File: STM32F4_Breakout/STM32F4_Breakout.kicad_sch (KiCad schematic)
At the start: 28 parts

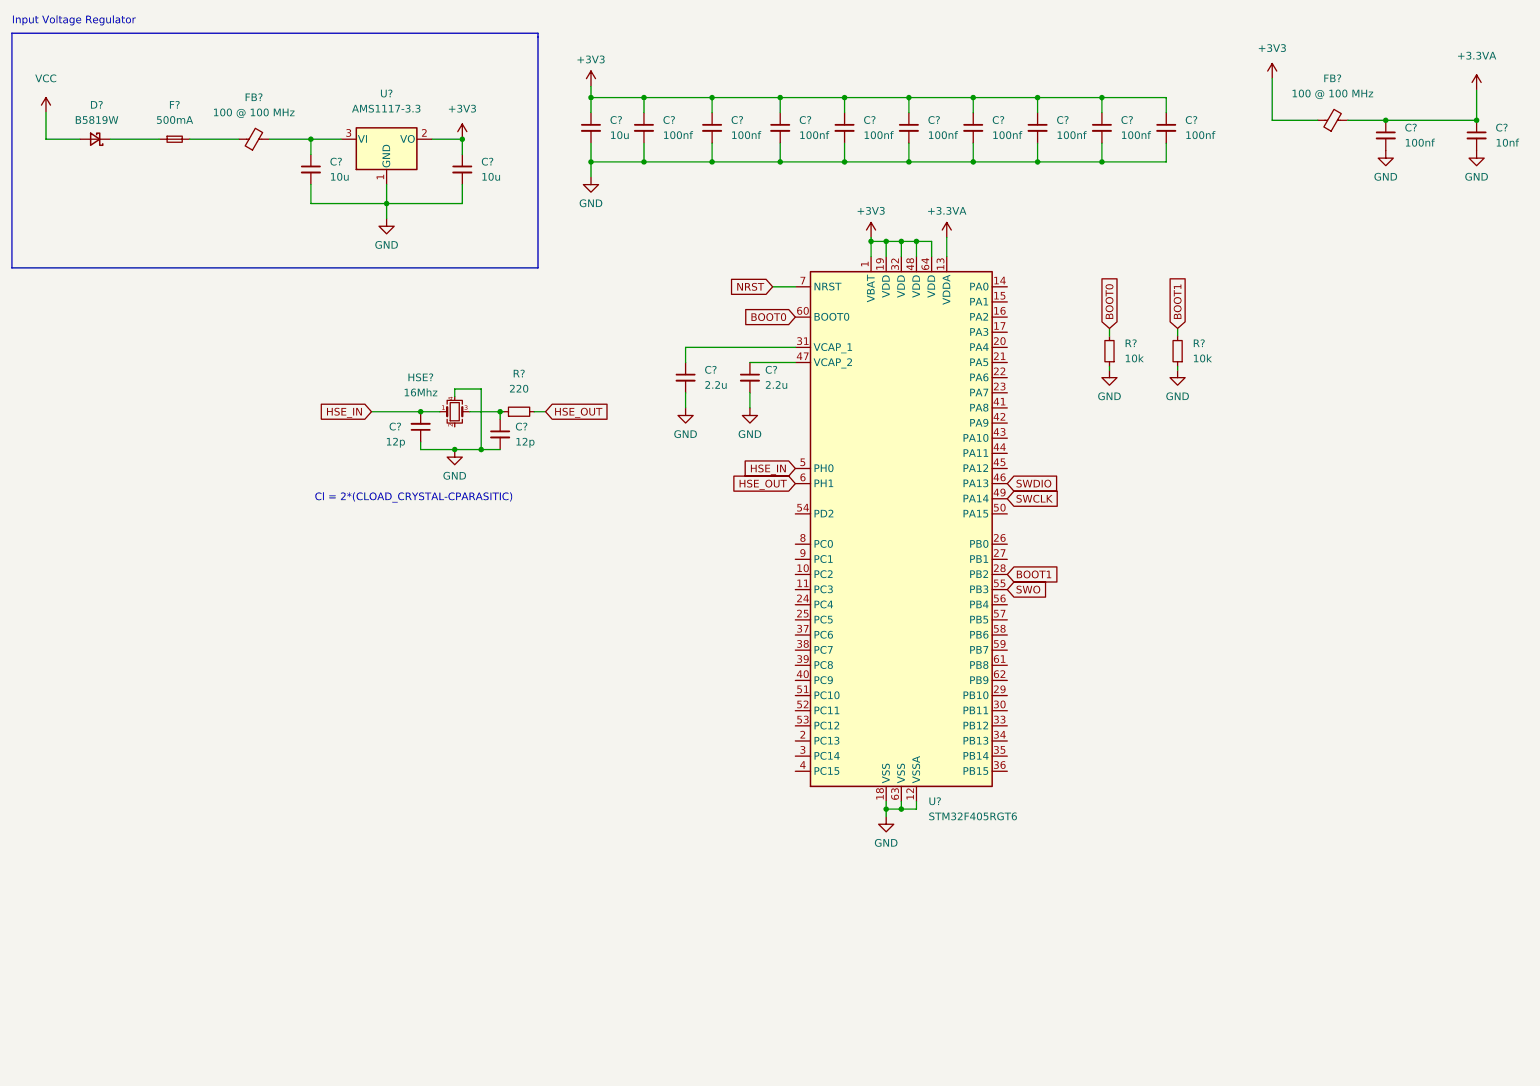
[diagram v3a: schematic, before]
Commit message: serial wire debug; pin assignments and peripheral selection in CubeMX
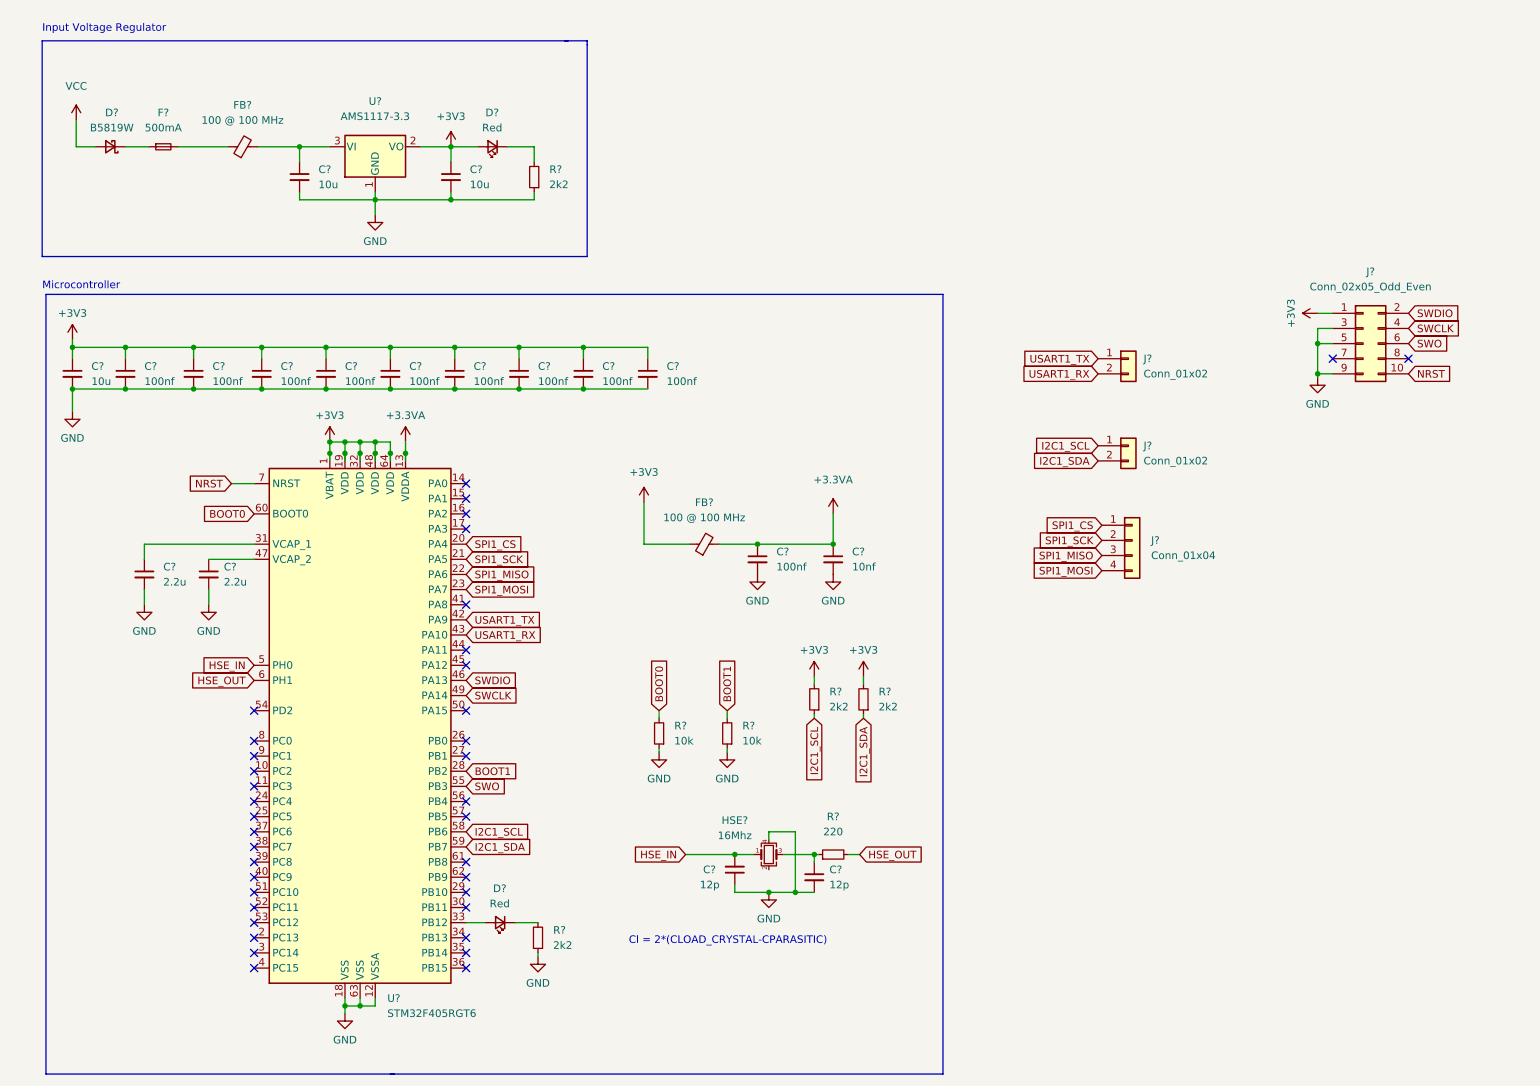
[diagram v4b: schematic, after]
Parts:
- added D? (x2): Red, symbol Device:LED_Small
- added J?: Conn_02x05_Odd_Even, symbol Connector_Generic:Conn_02x05_Odd_Even
- added J? (x2): Conn_01x02, symbol Connector_Generic:Conn_01x02
- added J?: Conn_01x04, symbol Connector_Generic:Conn_01x04
- added R? (x4): 2k2, symbol Device:R_Small
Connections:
- net +3V3: now also D?.2 (A), J?.1 (Pin_1), R?.2, R?.2
- net GND: now also J?.3 (Pin_3), J?.5 (Pin_5), J?.9 (Pin_9), R?.1, R?.1
- net NRST: now also J?.10 (Pin_10)
- net SWCLK: now also J?.4 (Pin_4)
- net SWDIO: now also J?.2 (Pin_2)
- net SWO: now also J?.6 (Pin_6)
- net SPI1_CS: now reaches U?.20 (PA4)
- net SPI1_CS: now also J?.1 (Pin_1)
- net SPI1_SCK: now reaches U?.21 (PA5)
- net SPI1_SCK: now also J?.2 (Pin_2)
- net SPI1_MISO: now reaches U?.22 (PA6)
- net SPI1_MISO: now also J?.3 (Pin_3)
- net SPI1_MOSI: now reaches U?.23 (PA7)
- net SPI1_MOSI: now also J?.4 (Pin_4)
- net at U?.33 (PB12): now also D?.2 (A)
- net USART1_TX: now reaches U?.42 (PA9)
- net USART1_TX: now also J?.1 (Pin_1)
- net USART1_RX: now reaches U?.43 (PA10)
- net USART1_RX: now also J?.2 (Pin_2)
- net I2C1_SCL: now reaches U?.58 (PB6)
- net I2C1_SCL: now also J?.1 (Pin_1), R?.1
- net I2C1_SDA: now reaches U?.59 (PB7)
- net I2C1_SDA: now also J?.2 (Pin_2), R?.1
- new net: D?.1 (K), R?.2 (x2)
- no-connect marks 0 -> 38
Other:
- note added: "Microcontroller"
- moved on the sheet: C?, D?, F?, FB?, HSE?, R?, U?

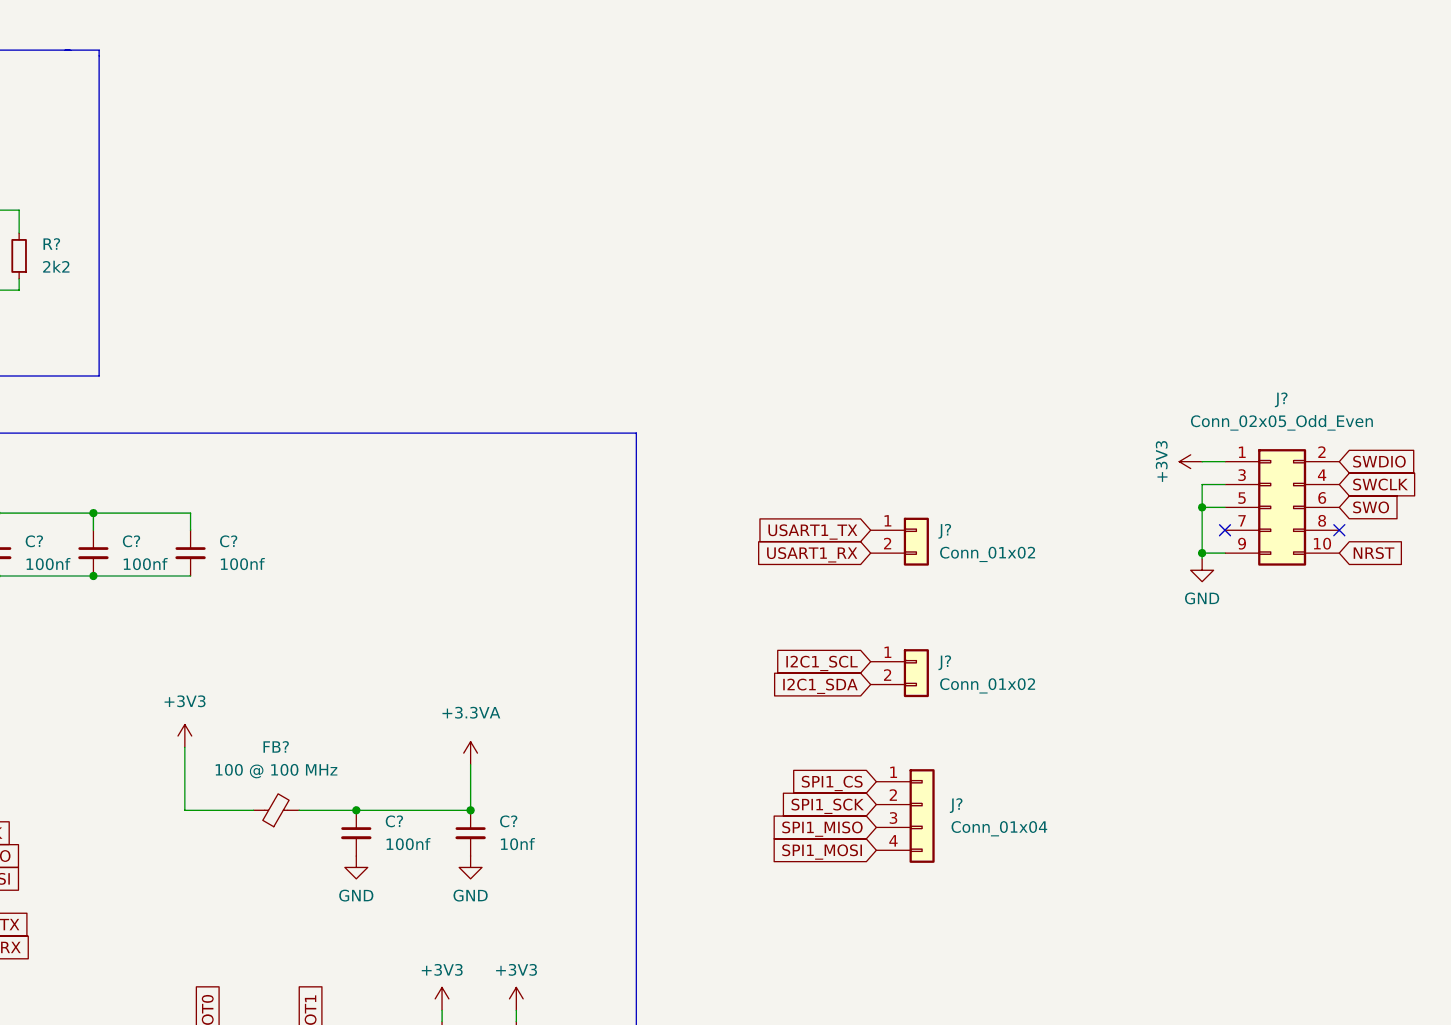
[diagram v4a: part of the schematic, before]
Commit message: adding connectors, test points and mounting holes
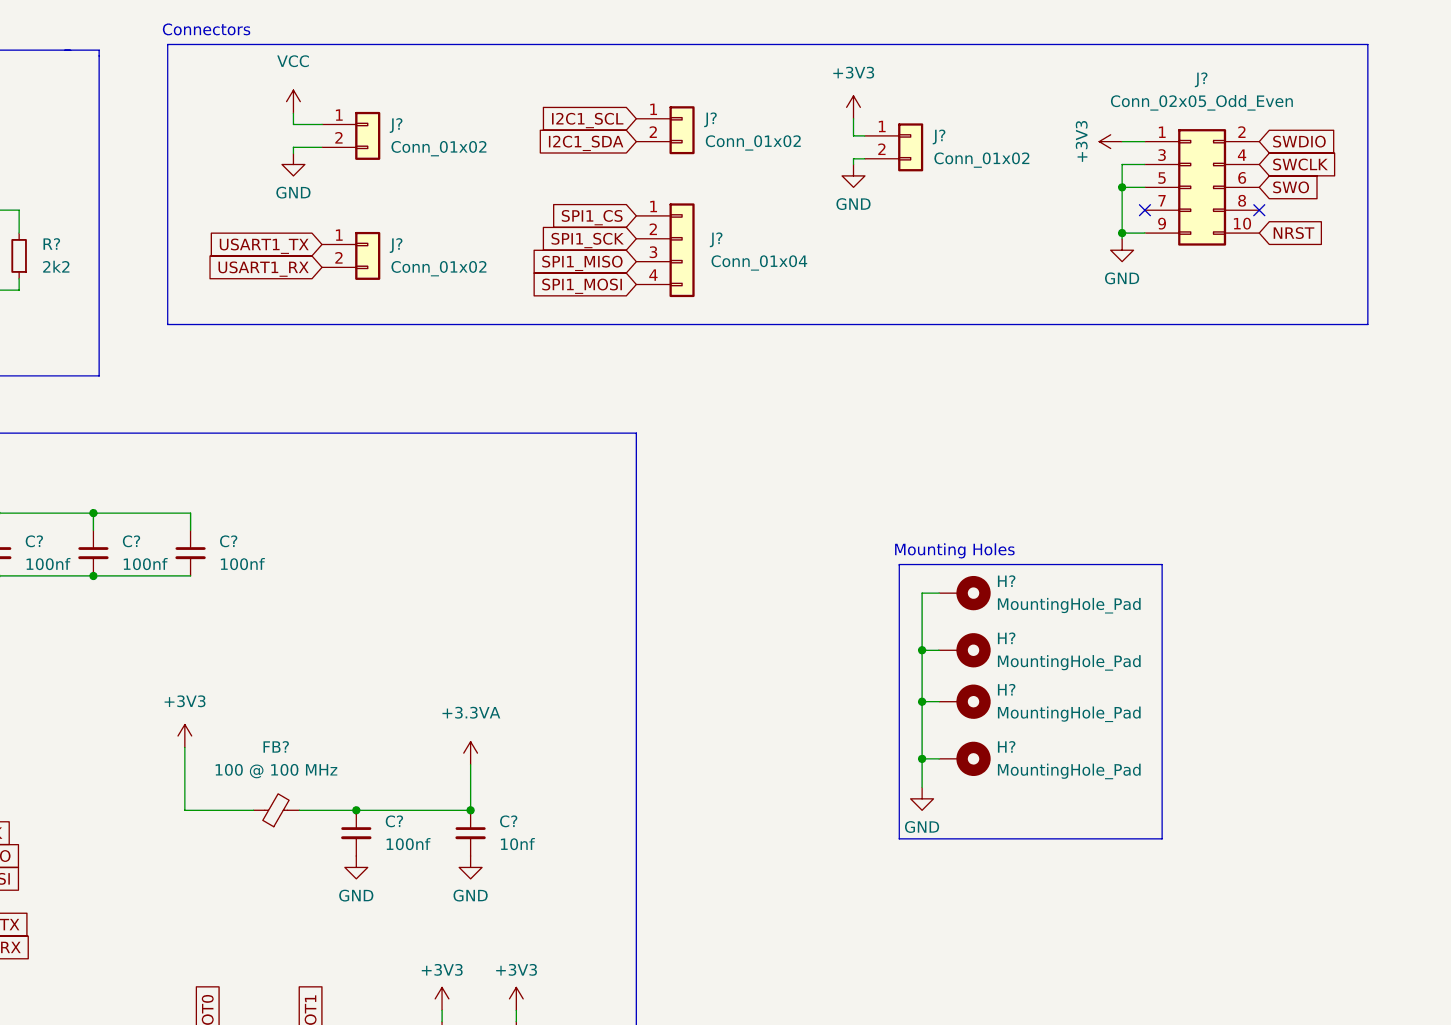
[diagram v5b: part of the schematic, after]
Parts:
- added H? (x4): MountingHole_Pad, symbol Mechanical:MountingHole_Pad
- added J? (x2): Conn_01x02, symbol Connector_Generic:Conn_01x02
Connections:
- net +3V3: now also J?.1 (Pin_1)
- net GND: now also H?.1, H?.1, H?.1, H?.1, J?.2 (Pin_2), J?.2 (Pin_2)
- net VCC: now also J?.1 (Pin_1)
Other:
- note added: "Connectors"
- note added: "Mounting Holes"
- moved on the sheet: J?

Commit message: adding labels, annotation and running ERC
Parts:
- gave numbers to parts that had none: 44
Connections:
- net GND: now also C1.1, HSE1.2; no longer C1.2
- net at FB1.2, U1.3 (VI): now also C1.2; no longer C1.1
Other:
- moved on the sheet: C1, C15, C16, D1, F1, FB1

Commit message: Component/footprint sizing, selection and assignment
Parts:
- C1, C2: footprint (none) -> Capacitor_SMD:C_0805_2012Metric
- C10, C11, C12, C13, C14, C17, C18, C4, C5, C6, C7, C8, C9: footprint (none) -> Capacitor_SMD:C_0402_1005Metric
- C15, C16, C3: footprint (none) -> Capacitor_SMD:C_0603_1608Metric
- D1: footprint (none) -> Diode_SMD:D_SOD-123
- D2, D3: footprint (none) -> LED_SMD:LED_0603_1608Metric
- F1: footprint (none) -> Fuse:Fuse_0603_1608Metric
- FB1, FB2: footprint (none) -> Inductor_SMD:L_0805_2012Metric
- H1, H2, H3, H4: footprint (none) -> MountingHole:MountingHole_4.3mm_M4_Pad_Via
- HSE1: footprint (none) -> Crystal:Crystal_SMD_3225-4Pin_3.2x2.5mm
- J1, J2, J3, J6: footprint (none) -> Connector_PinHeader_2.54mm:PinHeader_1x02_P2.54mm_Vertical
- J4: footprint (none) -> Connector_PinHeader_1.27mm:PinHeader_2x05_P1.27mm_Vertical_SMD
- J5: footprint (none) -> Connector_PinHeader_2.54mm:PinHeader_1x04_P2.54mm_Vertical
- R1, R7: footprint (none) -> Resistor_SMD:R_0603_1608Metric
- R2, R3, R4, R5, R6: footprint (none) -> Resistor_SMD:R_0402_1005Metric

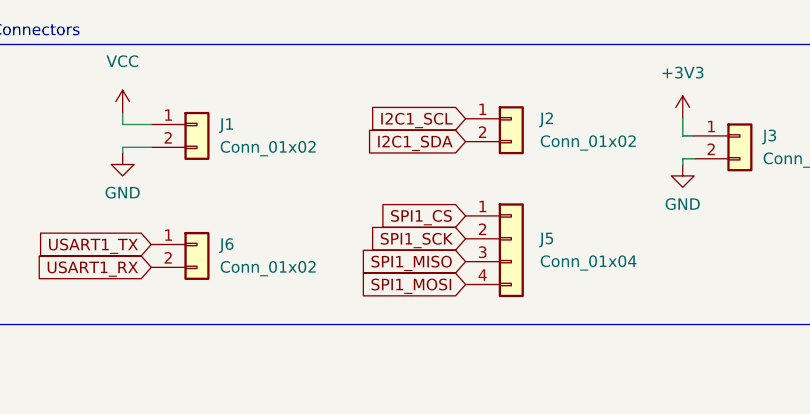
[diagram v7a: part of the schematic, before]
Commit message: setting up layers and design rules per jlcpcb
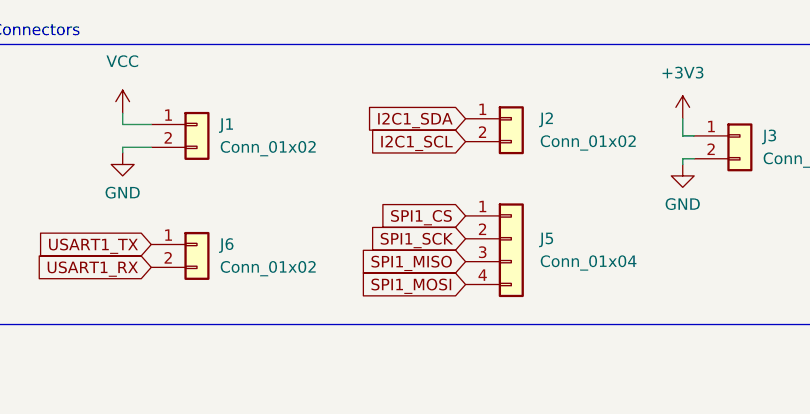
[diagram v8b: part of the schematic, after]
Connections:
- net I2C1_SCL: now also J2.2 (Pin_2); no longer J2.1 (Pin_1)
- net I2C1_SDA: now also J2.1 (Pin_1); no longer J2.2 (Pin_2)
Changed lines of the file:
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@@
+    )
+  )
+  (global_label "I2C1_SDA" (shape input) (at 170.815 26.67 180) (fields_autoplaced)
+    (effects (font (size 1.27 1.27)) (justify right))
+    (property "Intersheet References" "${INTERSHEET_REFS}" (id 0) (at 159.5724 26.7494 0)
+      (effects (font (size 1.27 1.27)) (justify right) hide)
     )
   )
@@
     )
   )
-  (global_label "I2C1_SDA" (shape input) (at 170.815 29.21 180) (fields_autoplaced)
+  (global_label "I2C1_SCL" (shape input) (at 170.815 29.21 180) (fields_autoplaced)
     (effects (font (size 1.27 1.27)) (justify right))
-    (property "Intersheet References" "${INTERSHEET_REFS}" (id 0) (at 159.5724 29.2894 0)
+    (property "Intersheet References" "${INTERSHEET_REFS}" (id 0) (at 159.6329 29.2894 0)
       (effects (font (size 1.27 1.27)) (justify right) hide)
     )
@@
       (effects (font (size 1.27 1.27)) (justify right) hide)
     )
-  )
-  (global_label "I2C1_SCL" (shape input) (at 170.815 26.67 180) (fields_autoplaced)
-    (effects (font (size 1.27 1.27)) (justify right))
-    (property "Intersheet References" "${INTERSHEET_REFS}" (id 0) (at 159.6329 26.7494 0)
-      (effects (font (size 1.27 1.27)) (justify right) hide)
-    )
